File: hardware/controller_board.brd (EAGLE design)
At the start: 144 x 118 mm, 51 parts, among them J1 FRSKY-GIMBAL, J2 FRSKY-GIMBAL, J3 WIRE-HARNESS-SPARKFUN-9915, J4 AVR_SPI_PRG_6NS, J7 FTDI_BASICPTH, SW1 PUSHBUTTON_SMD-VERTICAL-1, SW2 PUSHBUTTON_SMD-VERTICAL-1, SW3 PUSHBUTTON_SMD-VERTICAL-1, SW4 PUSHBUTTON_SMD-VERTICAL-1, SW5 PUSHBUTTON_SMD-VERTICAL-1, U1 ATMEGA128RFA1, U2 TPS73633-DBVT, Y1 CRYSTAL5X3

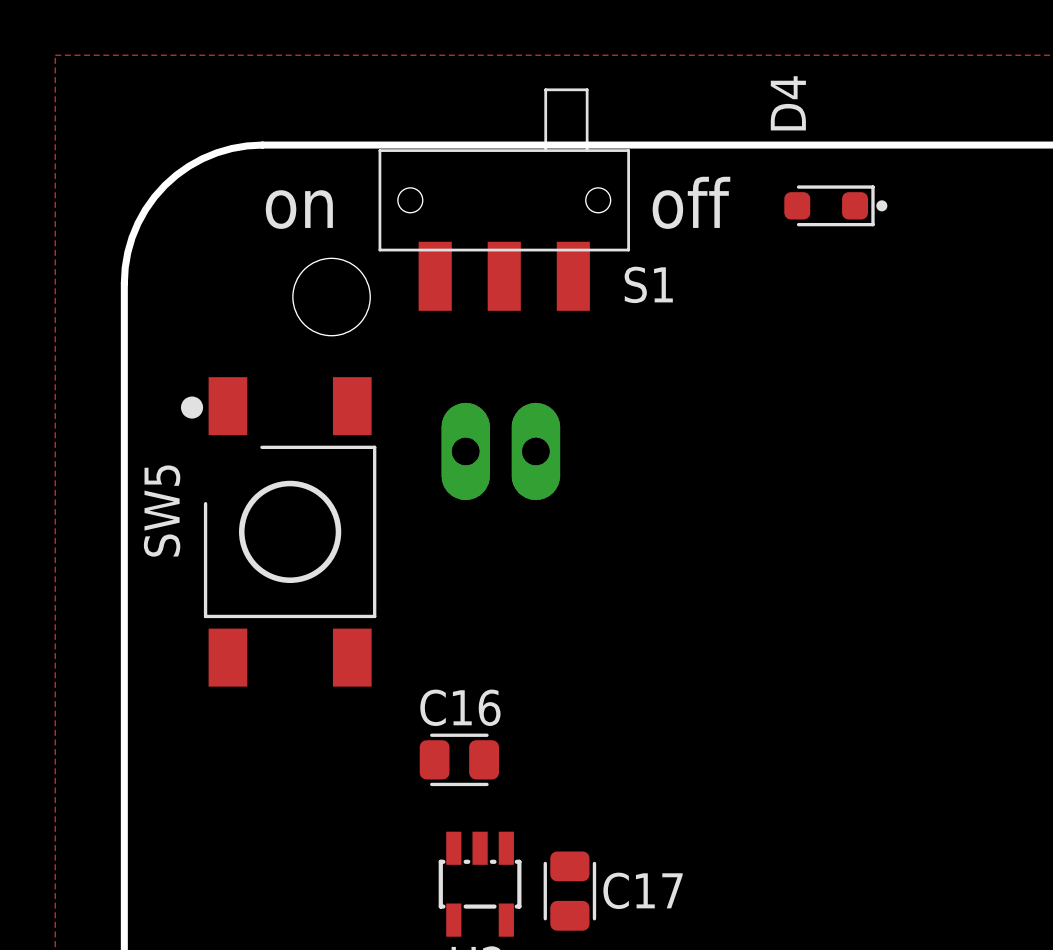
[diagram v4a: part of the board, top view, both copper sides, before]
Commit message: move power switch out of the way
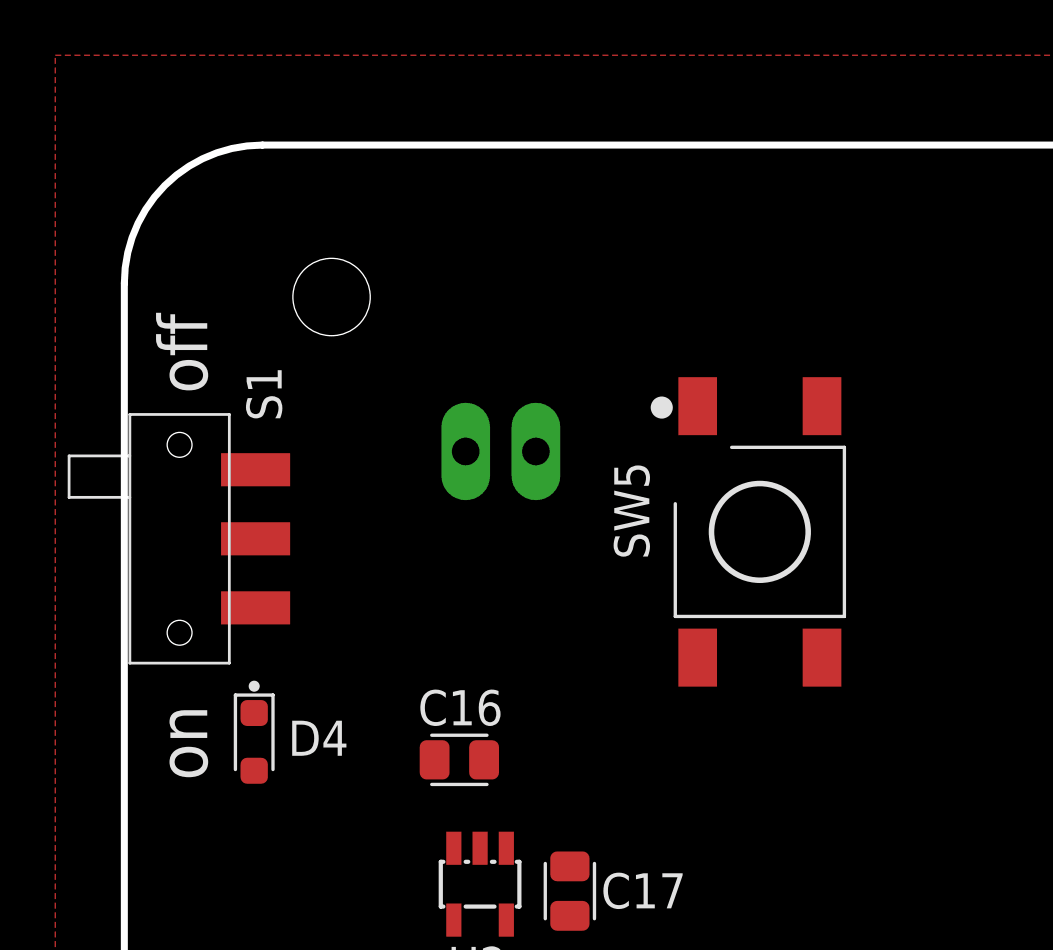
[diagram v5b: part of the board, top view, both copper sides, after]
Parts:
- moved D4 29.6 mm to (-68.2, 35.7), turned to 90 degrees
- moved SW5 17.0 mm to (-49.0, 44.0)
- moved S1 17.0 mm to (-70.0, 43.8), turned to 270 degrees
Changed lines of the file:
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@@
 <setting verticaltext="up"/>
 </settings>
-<grid distance="1" unitdist="mm" unit="mm" style="lines" multiple="1" display="yes" altdistance="0.001" altunitdist="mm" altunit="mm"/>
+<grid distance="0.5" unitdist="mm" unit="mm" style="lines" multiple="1" display="yes" altdistance="0.001" altunitdist="mm" altunit="mm"/>
 <layers>
 <layer number="1" name="Top" color="4" fill="1" visible="yes" active="yes"/>
@@
 <layer number="18" name="Vias" color="2" fill="1" visible="yes" active="yes"/>
 <layer number="19" name="Unrouted" color="12" fill="1" visible="yes" active="yes"/>
-<layer number="20" name="Dimension" color="15" fill="1" visible="yes" active="yes"/>
+<layer number="20" name="Dimension" color="15" fill="1" visible="no" active="yes"/>
 <layer number="21" name="tPlace" color="7" fill="1" visible="yes" active="yes"/>
 <layer number="22" name="bPlace" color="7" fill="1" visible="yes" active="yes"/>
@@
 <wire x1="-10.4" y1="36.5" x2="-10.6" y2="36.7" width="0.127" layer="39"/>
 <wire x1="-10.6" y1="36.7" x2="-11.7" y2="36.7" width="0.127" layer="39"/>
-<text x="-53" y="55" size="1.778" layer="21" font="vector">off</text>
-<text x="-67" y="55" size="1.778" layer="21" font="vector">on</text>
+<text x="-69" y="49" size="1.778" layer="21" font="vector" rot="R90">off</text>
+<text x="-69" y="35" size="1.778" layer="21" font="vector" rot="R90">on</text>
 </plain>
 <attributes>
@@
 <attribute name="VALUE" x="-28.65" y="-9.905" size="1.27" layer="27" font="vector" rot="R90"/>
 </element>
-<element name="S1" library="RemoteParts" package="JS102011SAQN" value="POWER-SWITCH-MFS201N-9-ZJS102011SAQN" x="-58.25" y="56" smashed="yes" rot="R180">
-<attribute name="NAME" x="-53" y="52.94" size="1.27" layer="21" font="vector" align="center"/>
-</element>
-<element name="D4" library="quadparts_prebuilt" package="LEDSC125X200X120-2_HS" value="green" x="-47.3" y="56.7" smashed="yes">
-<attribute name="CREATOR" value="Swanson" x="-47.3" y="56.7" size="1.778" layer="27" display="off"/>
-<attribute name="DIST" value="Digikey" x="-47.3" y="56.7" size="1.778" layer="27" display="off"/>
-<attribute name="DISTPN" value="160-1179-1-ND" x="-47.3" y="56.7" size="1.778" layer="27" display="off"/>
-<attribute name="MFR" value="Lite-On Inc" x="-47.3" y="56.7" size="1.778" layer="27" display="off"/>
-<attribute name="MPN" value="LTST-C170GKT" x="-47.3" y="56.7" size="1.778" layer="27" display="off"/>
-<attribute name="NAME" x="-47.3334" y="58.375" size="1.27" layer="25" font="vector" ratio="10" rot="R90"/>
-<attribute name="REVIEWER" value="Swanson" x="-47.3" y="56.7" size="1.778" layer="27" display="off"/>
-<attribute name="VALUE" value="green" x="-44.0996" y="54.8966" size="1.27" layer="27" font="vector" ratio="10"/>
+<element name="S1" library="RemoteParts" package="JS102011SAQN" value="POWER-SWITCH-MFS201N-9-ZJS102011SAQN" x="-70" y="43.75" smashed="yes" rot="R270">
+<attribute name="NAME" x="-66.94" y="49" size="1.27" layer="21" font="vector" rot="R90" align="center"/>
+</element>
+<element name="D4" library="quadparts_prebuilt" package="LEDSC125X200X120-2_HS" value="green" x="-68.2" y="35.7" smashed="yes" rot="R90">
+<attribute name="CREATOR" value="Swanson" x="-68.2" y="35.7" size="1.778" layer="27" rot="R90" display="off"/>
+<attribute name="DIST" value="Digikey" x="-68.2" y="35.7" size="1.778" layer="27" rot="R90" display="off"/>
+<attribute name="DISTPN" value="160-1179-1-ND" x="-68.2" y="35.7" size="1.778" layer="27" rot="R90" display="off"/>
+<attribute name="MFR" value="Lite-On Inc" x="-68.2" y="35.7" size="1.778" layer="27" rot="R90" display="off"/>
+<attribute name="MPN" value="LTST-C170GKT" x="-68.2" y="35.7" size="1.778" layer="27" rot="R90" display="off"/>
+<attribute name="NAME" x="-63.875" y="37.1666" size="1.27" layer="25" font="vector" ratio="10" rot="R180"/>
+<attribute name="REVIEWER" value="Swanson" x="-68.2" y="35.7" size="1.778" layer="27" rot="R90" display="off"/>
+<attribute name="VALUE" value="green" x="-66.3966" y="38.9004" size="1.27" layer="27" font="vector" ratio="10" rot="R90"/>
 </element>
 <element name="J3" library="RemoteParts" package="WIRE-HARNESS-SPARKFUN-9915" value="WIRE-HARNESS-SPARKFUN-9915" x="19.5" y="12.25" rot="MR270">
@@
 <attribute name="REVIEWER" value="Swanson" x="50" y="-41" size="1.778" layer="27" font="vector" rot="R270" display="off"/>
 </element>
-<element name="SW5" library="quadparts_prebuilt" package="TE_FSM8JSMA_HS" value="PUSHBUTTON_SMD-VERTICAL-1" x="-66" y="44" smashed="yes">
-<attribute name="CREATOR" value="Swanson" x="-66" y="44" size="1.778" layer="27" font="vector" display="off"/>
-<attribute name="DIST" value="Digikey" x="-66" y="44" size="1.778" layer="27" font="vector" display="off"/>
-<attribute name="DISTPN" value="450-1129-ND" x="-66" y="44" size="1.778" layer="27" font="vector" display="off"/>
-<attribute name="MFR" value="TE Connectivity Alcoswitch Switches" x="-66" y="44" size="1.778" layer="27" font="vector" display="off"/>
-<attribute name="MPN" value="FSM4JSMA" x="-66" y="44" size="1.778" layer="27" font="vector" display="off"/>
-<attribute name="NAME" x="-70" y="43" size="1.27" layer="25" font="vector" rot="R90"/>
-<attribute name="REVIEWER" value="Swanson" x="-66" y="44" size="1.778" layer="27" font="vector" display="off"/>
+<element name="SW5" library="quadparts_prebuilt" package="TE_FSM8JSMA_HS" value="PUSHBUTTON_SMD-VERTICAL-1" x="-49" y="44" smashed="yes">
+<attribute name="CREATOR" value="Swanson" x="-49" y="44" size="1.778" layer="27" font="vector" display="off"/>
+<attribute name="DIST" value="Digikey" x="-49" y="44" size="1.778" layer="27" font="vector" display="off"/>
+<attribute name="DISTPN" value="450-1129-ND" x="-49" y="44" size="1.778" layer="27" font="vector" display="off"/>
+<attribute name="MFR" value="TE Connectivity Alcoswitch Switches" x="-49" y="44" size="1.778" layer="27" font="vector" display="off"/>
+<attribute name="MPN" value="FSM4JSMA" x="-49" y="44" size="1.778" layer="27" font="vector" display="off"/>
+<attribute name="NAME" x="-53" y="43" size="1.27" layer="25" font="vector" rot="R90"/>
+<attribute name="REVIEWER" value="Swanson" x="-49" y="44" size="1.778" layer="27" font="vector" display="off"/>
 </element>
 </elements>
@@
 <contactref element="SW5" pad="3"/>
 <contactref element="SW5" pad="4"/>
-<wire x1="-63.75" y1="48.55" x2="-63.75" y2="39.45" width="0" layer="19" extent="1-1"/>
-<wire x1="-66" y1="-10" x2="-63.75" y2="48.55" width="0" layer="19" extent="1-1"/>
+<wire x1="-46.75" y1="48.55" x2="-46.75" y2="39.45" width="0" layer="19" extent="1-1"/>
+<wire x1="-66" y1="-10" x2="-46.75" y2="48.55" width="0" layer="19" extent="1-1"/>
 <wire x1="-66" y1="-4" x2="-66" y2="-10" width="0" layer="19" extent="1-1"/>
 <wire x1="-54.55" y1="-27.25" x2="-66" y2="-10" width="0" layer="19" extent="1-1"/>
@@
 <wire x1="-59.125" y1="32.55" x2="-55.875" y2="31.895" width="0" layer="19" extent="1-1"/>
 <wire x1="-58.98" y1="35.75" x2="-59.125" y2="32.55" width="0" layer="19" extent="1-1"/>
-<wire x1="-45.555" y1="55.8" x2="-58.98" y2="35.75" width="0" layer="19" extent="1-1"/>
-<wire x1="-57.105" y1="46.91" x2="-45.555" y2="55.8" width="0" layer="19" extent="1-1"/>
+<wire x1="-67.3" y1="37.445" x2="-58.98" y2="35.75" width="0" layer="19" extent="1-1"/>
+<wire x1="-57.105" y1="46.91" x2="-67.3" y2="37.445" width="0" layer="19" extent="1-1"/>
 </signal>
 <signal name="BTN1">
@@
 <contactref element="J5" pad="1"/>
 <contactref element="J6" pad="2"/>
-<wire x1="40.33" y1="54.5" x2="-47.645" y2="55.8" width="0" layer="19" extent="1-1"/>
+<wire x1="40.33" y1="54.5" x2="-67.3" y2="35.355" width="0" layer="19" extent="1-1"/>
 <wire x1="37.79" y1="54.5" x2="40.33" y2="54.5" width="0" layer="19" extent="1-1"/>
 <wire x1="35.25" y1="54.5" x2="37.79" y2="54.5" width="0" layer="19" extent="1-1"/>
@@
 <wire x1="-26.23" y1="38.125" x2="-22.881" y2="38" width="0" layer="19" extent="1-1"/>
 <wire x1="-26.75" y1="35.895" x2="-26.23" y2="38.125" width="0" layer="19" extent="1-1"/>
-<wire x1="49.5" y1="23.25" x2="-47.645" y2="55.8" width="0" layer="19" extent="1-1"/>
+<wire x1="49.5" y1="23.25" x2="-67.3" y2="35.355" width="0" layer="19" extent="1-1"/>
 <wire x1="49.045" y1="18.25" x2="49.5" y2="23.25" width="0" layer="19" extent="1-1"/>
 <wire x1="-55.875" y1="30.105" x2="-26.75" y2="35.895" width="0" layer="19" extent="1-1"/>
@@
 <contactref element="SW5" pad="2"/>
 <contactref element="SW5" pad="1"/>
-<wire x1="-68.25" y1="48.55" x2="-68.25" y2="39.45" width="0" layer="19" extent="1-1"/>
-<wire x1="-19.75" y1="42.131" x2="-68.25" y2="48.55" width="0" layer="19" extent="1-1"/>
+<wire x1="-51.25" y1="48.55" x2="-51.25" y2="39.45" width="0" layer="19" extent="1-1"/>
+<wire x1="-19.75" y1="42.131" x2="-51.25" y2="48.55" width="0" layer="19" extent="1-1"/>
 <wire x1="23.35" y1="42.355" x2="-19.75" y2="42.131" width="0" layer="19" extent="1-1"/>
 <wire x1="25.725" y1="40.48" x2="23.35" y2="42.355" width="0" layer="19" extent="1-1"/>
@@
 <wire x1="-60.075" y1="32.55" x2="-58.175" y2="32.55" width="0" layer="19" extent="1-1"/>
 <wire x1="-60.77" y1="35.75" x2="-60.075" y2="32.55" width="0" layer="19" extent="1-1"/>
-<wire x1="-58.25" y1="53.25" x2="-60.77" y2="35.75" width="0" layer="19" extent="1-1"/>
-<wire x1="-69.25" y1="39.75" x2="-58.25" y2="53.25" width="0" layer="19" extent="1-1"/>
+<wire x1="-67.25" y1="43.75" x2="-60.77" y2="35.75" width="0" layer="19" extent="1-1"/>
+<wire x1="-69.25" y1="39.75" x2="-67.25" y2="43.75" width="0" layer="19" extent="1-1"/>
 </signal>
 <signal name="N$1">
 <contactref element="BATT5" pad="+"/>
 <contactref element="S1" pad="P$1"/>
-<wire x1="-60.75" y1="53.25" x2="-69.25" y2="43.75" width="0" layer="19" extent="1-1"/>
-<wire x1="-59.645" y1="46.91" x2="-60.75" y2="53.25" width="0" layer="19" extent="1-1"/>
+<wire x1="-67.25" y1="41.25" x2="-69.25" y2="43.75" width="0" layer="19" extent="1-1"/>
+<wire x1="-59.645" y1="46.91" x2="-67.25" y2="41.25" width="0" layer="19" extent="1-1"/>
 </signal>
 <signal name="N$5">

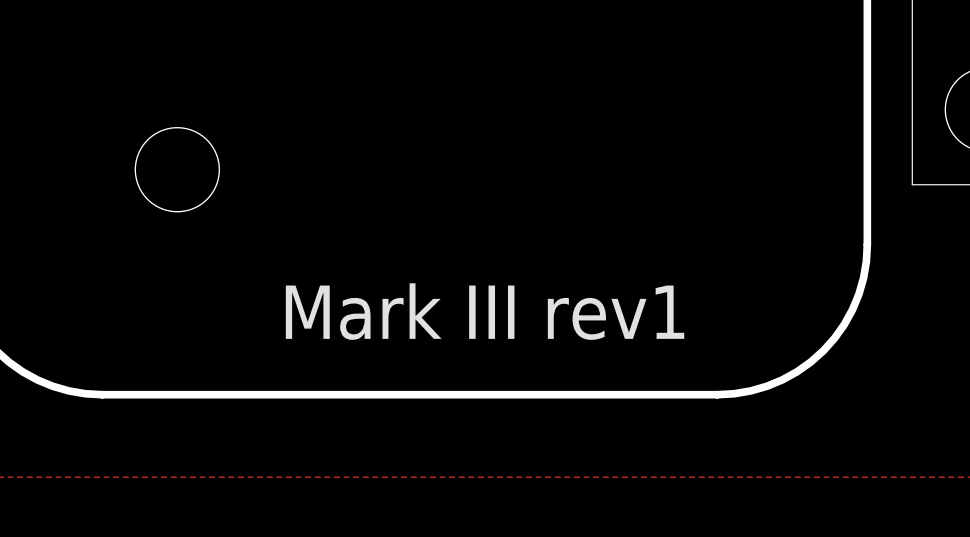
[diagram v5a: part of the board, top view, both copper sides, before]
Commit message: use 3.3V regulator
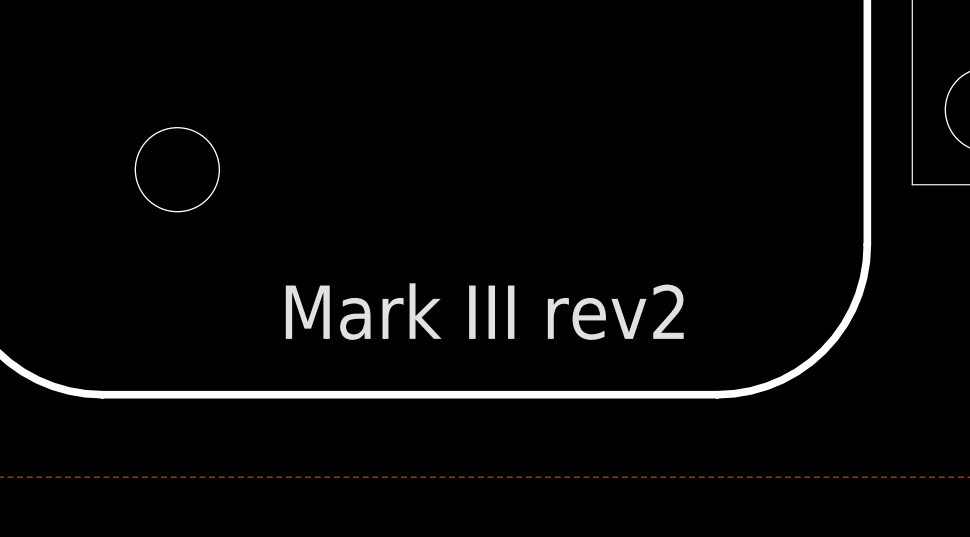
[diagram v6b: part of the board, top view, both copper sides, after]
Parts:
- U2: value TPS73633-DBVT -> TPS73633-DBVT3.3V
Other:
- board text added: "Mark III rev2"
- board text removed: "Mark III rev1"
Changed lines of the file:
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@@
 <wire x1="-46.5" y1="-60" x2="-41.5" y2="-55" width="0.254" layer="20" curve="90"/>
 <dimension x1="-72" y1="53" x2="72" y2="51.5" x3="0" y3="62.5" textsize="1.778" layer="47" dtype="horizontal" unit="inch"/>
-<text x="-54.25" y="-57.25" size="1.778" layer="21" font="vector" align="center">Mark III rev1</text>
+<text x="-54.25" y="-57.25" size="1.778" layer="21" font="vector" align="center">Mark III rev2</text>
 <text x="44.75" y="-58.25" size="1.778" layer="21" font="vector">Steven Swanson</text>
 <dimension x1="-67" y1="58" x2="-62.5" y2="-60" x3="-77.5" y3="-1" textsize="1.778" layer="47" dtype="vertical" unit="inch"/>
@@
 <attribute name="VALUE" x="-55.875" y="31" size="1.2" layer="27" font="vector" ratio="10" rot="R270"/>
 </element>
-<element name="U2" library="quadparts_prebuilt" package="SOT23-DBV" value="TPS73633-DBVT" x="-59.125" y="31.25" rot="R180">
+<element name="U2" library="quadparts_prebuilt" package="SOT23-DBV" value="TPS73633-DBVT3.3V" x="-59.125" y="31.25" rot="R180">
 <attribute name="CREATOR" value="Swanson" x="-46.625" y="39.25" size="1.778" layer="27" rot="R180" display="off"/>
-<attribute name="DATASHEET" value="http://www.ti.com/lit/ds/symlink/lp3985.pdf" x="-46.625" y="39.25" size="1.778" layer="27" rot="R180" display="off"/>
-<attribute name="DIST" value="Digikey" x="-46.625" y="39.25" size="1.778" layer="27" rot="R180" display="off"/>
-<attribute name="DISTPN" value="LP3985IM5X-3.0/NOPBCT-ND" x="-46.625" y="39.25" size="1.778" layer="27" rot="R180" display="off"/>
-<attribute name="MFR" value="Texas Instruments" x="-46.625" y="39.25" size="1.778" layer="27" rot="R180" display="off"/>
-<attribute name="MPN" value="LP3985IM5X-3.0/NOPB" x="-46.625" y="39.25" size="1.778" layer="27" rot="R180" display="off"/>
-<attribute name="PRICE" value="0.59" x="-46.625" y="39.25" size="1.778" layer="27" rot="R180" display="off"/>
-<attribute name="REVIEWER" value="Swanson" x="-46.625" y="39.25" size="1.778" layer="27" rot="R180" display="off"/>
+<attribute name="DIST" value="DIGIKEY" x="-46.625" y="39.25" size="1.778" layer="27" rot="R180" display="off"/>
+<attribute name="DISTPN" value="LP3985IM5‑3.3/NOPBCT‑ND" x="-46.625" y="39.25" size="1.778" layer="27" rot="R180" display="off"/>
 </element>
 <element name="R4" library="quadparts_prebuilt" package="RESC2012X60_HS" value="10K" x="50" y="18.25" locked="yes" smashed="yes" rot="R180">
